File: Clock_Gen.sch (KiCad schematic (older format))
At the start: 0 parts

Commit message: Added clock gen parts
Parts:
- added C?: C_Small, Capacitor_SMD:C_0603_1608Metric_Pad1.08x0.95mm_HandSolder, symbol Device:C_Small
- added C?: C_Polarized_Small, Capacitor_Tantalum_SMD:CP_EIA-1608-10_AVX-L_Pad1.25x1.05mm_HandSolder, symbol Device:C_Polarized_Small
- added C?: C_Small, symbol Device:C_Small
- added C? (x8): 100nF, Capacitor_SMD:C_0201_0603Metric_Pad0.64x0.40mm_HandSolder, symbol Device:C_Small
- added C? (x5): 1uF, Capacitor_SMD:C_0603_1608Metric_Pad1.08x0.95mm_HandSolder, symbol Device:C_Small
- added R?: R_Small_US, Resistor_SMD:R_0603_1608Metric_Pad0.98x0.95mm_HandSolder, symbol Device:R_Small_US
- added U?: Si5344A-D, Package_DFN_QFN:QFN-44-1EP_7x7mm_P0.5mm_EP5.2x5.2mm, symbol Timer_PLL:Si5344A-D
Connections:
- new net: C?.2, U?.19 (OUT0b)
- new net: C?.2, U?.20 (OUT0)
- new net: C?.2, U?.24 (OUT1b)
- new net: C?.2, U?.25 (OUT1)
- new net: C?.2, U?.30 (OUT2b)
- new net: C?.2, U?.31 (OUT2)
- new net: C?.2, U?.35 (OUT3b)
- new net: C?.2, U?.36 (OUT3)
- new net CLK_OUT0_N: C?.1
- new net CLK_OUT0_P: C?.1
- new net CLK_OUT1_N: C?.1
- new net CLK_OUT1_P: C?.1
- new net CLK_OUT2_N: C?.1
- new net CLK_OUT2_P: C?.1
- new net CLK_OUT3_N: C?.1
- new net CLK_OUT3_P: C?.1
- new net GNDD: C?.2, C?.2, C?.2, C?.2, C?.2
- new net VCC1V8: C?.1, C?.1, C?.1, C?.1, C?.1, U?.18 (VDDO0), U?.21 (VDD), U?.23 (VDDO1), U?.26 (VDDS), U?.29 (VDDO2), U?.32 (VDD), U?.34 (VDDO3), U?.39 (VDD), U?.40 (VDD)
- new net VCC3V3: U?.8 (VDDA), U?.9 (VDDA)

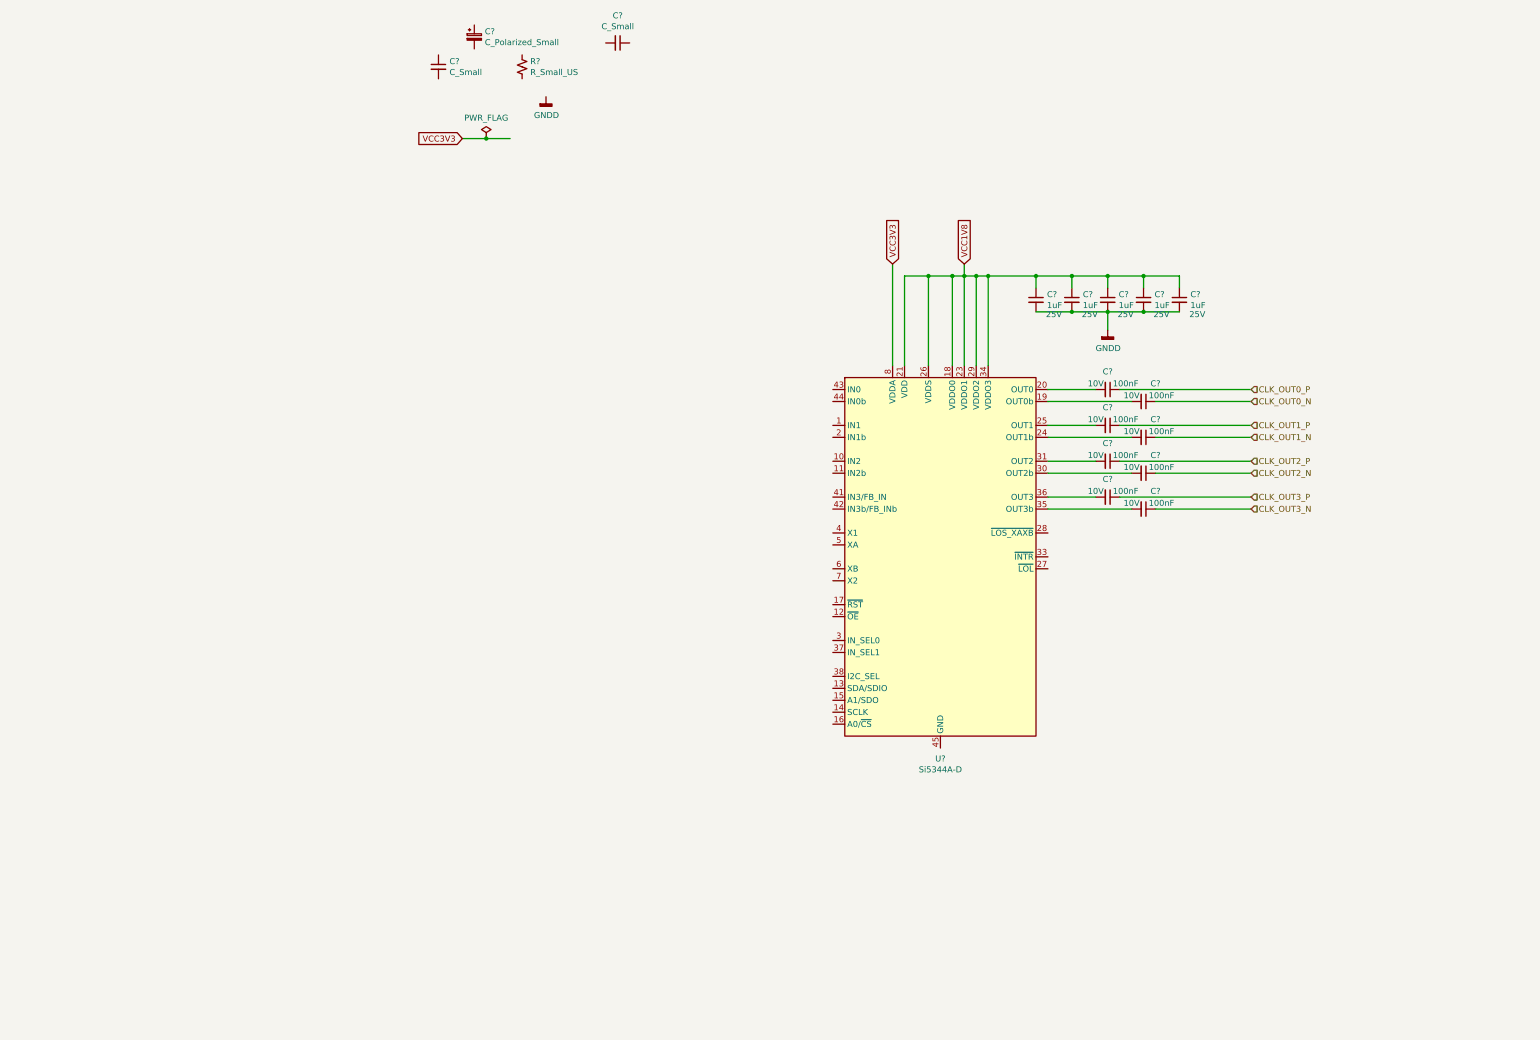
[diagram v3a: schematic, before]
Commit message: Drawn configuration cct of Ethernet PHY Drawn Clock Gen cct
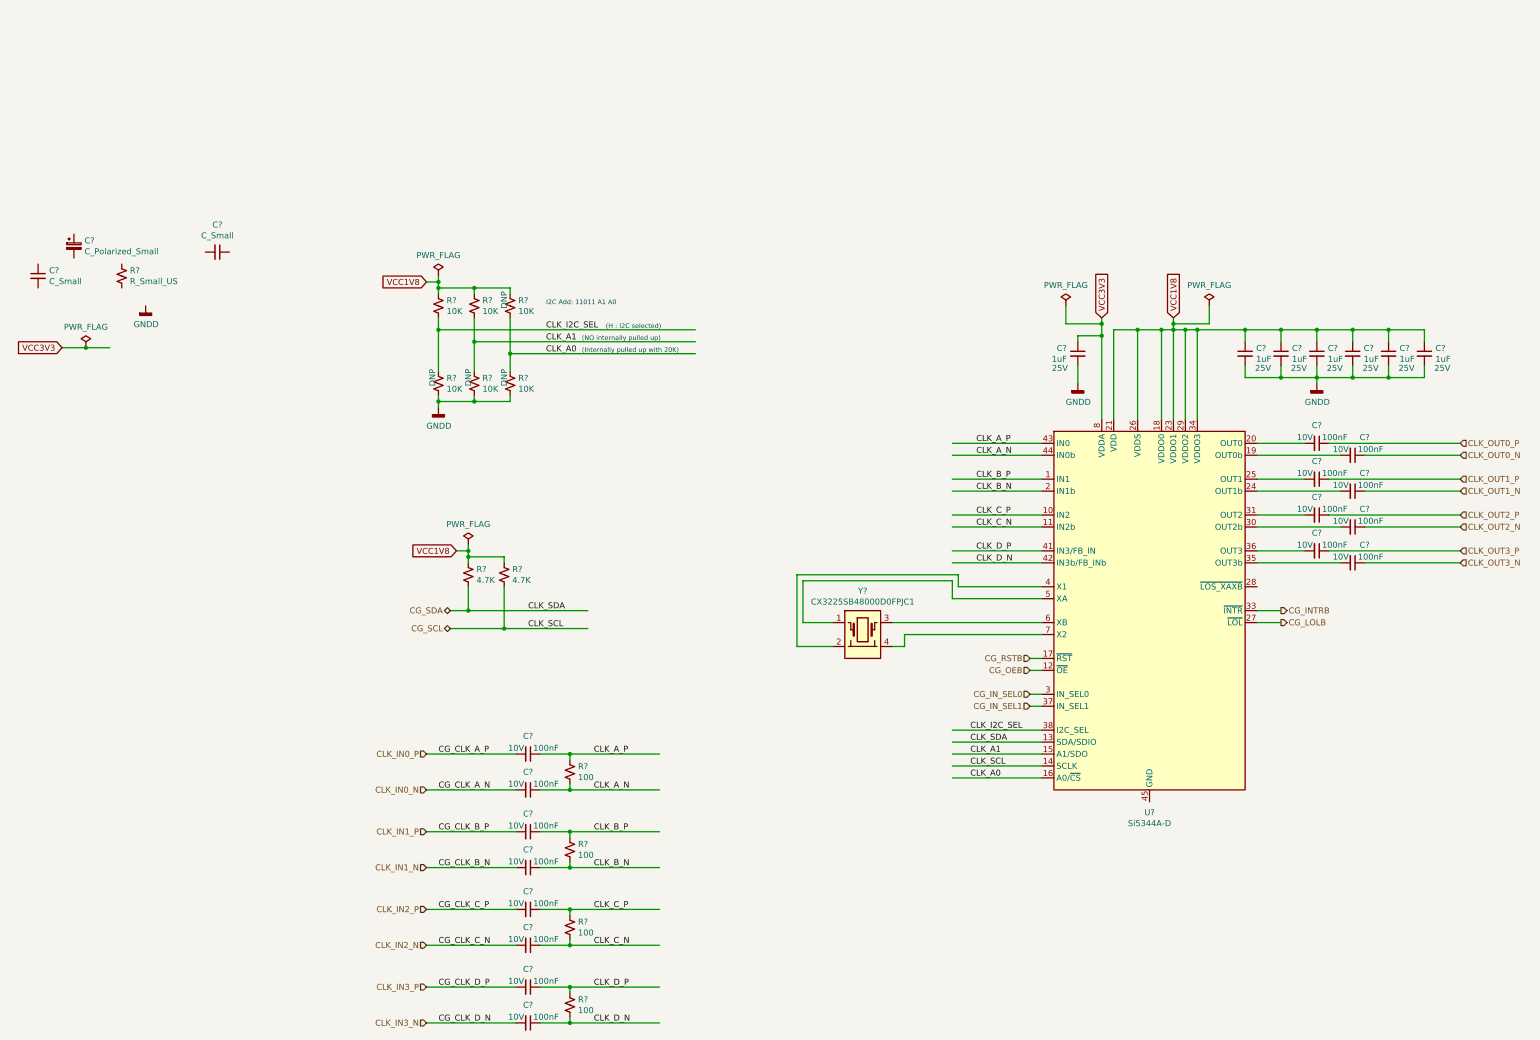
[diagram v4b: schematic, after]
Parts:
- added C? (x8): 100nF, Capacitor_SMD:C_0201_0603Metric_Pad0.64x0.40mm_HandSolder, symbol Device:C_Small
- added C? (x2): 1uF, Capacitor_SMD:C_0603_1608Metric_Pad1.08x0.95mm_HandSolder, symbol Device:C_Small
- added R? (x4): 100, Resistor_SMD:R_0603_1608Metric_Pad0.98x0.95mm_HandSolder, symbol Device:R_Small_US
- added R? (x6): 10K, Resistor_SMD:R_0603_1608Metric_Pad0.98x0.95mm_HandSolder, symbol Device:R_Small_US
- added R? (x2): 4.7K, Resistor_SMD:R_0603_1608Metric_Pad0.98x0.95mm_HandSolder, symbol Device:R_Small_US
- added Y?: CX3225SB48000D0FPJC1, GM_Crystals_Oscilators_n_Resonators:OSCCC320X250X60N, symbol GM_Crystals_Oscilators_n_Resonators:CX3225SB48000D0FPJC1
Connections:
- net labels added: CG_CLK_A_N, CG_CLK_A_P, CG_CLK_B_N, CG_CLK_B_P, CG_CLK_C_N, CG_CLK_C_P, CG_CLK_D_N, CG_CLK_D_P, CG_INTRB, CG_IN_SEL0, CG_IN_SEL1, CG_LOLB, CG_OEB, CG_RSTB, CG_SCL, CG_SDA, CLK_A0, CLK_A1, CLK_A_N, CLK_A_P, CLK_B_N, CLK_B_P, CLK_C_N, CLK_C_P, CLK_D_N, CLK_D_P, CLK_I2C_SEL, CLK_IN0_N, CLK_IN0_P, CLK_IN1_N, CLK_IN1_P, CLK_IN2_N, CLK_IN2_P, CLK_IN3_N, CLK_IN3_P, CLK_SCL, CLK_SDA
- wire segments 46 -> 165
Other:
- note added: "(H : I2C selected)"
- note added: "(Internally pulled up with 20K)"
- note added: "(NO internally pulled up)"
- note added: "I2C Add: 11011 A1 A0"
- moved on the sheet: C?, R?, U?

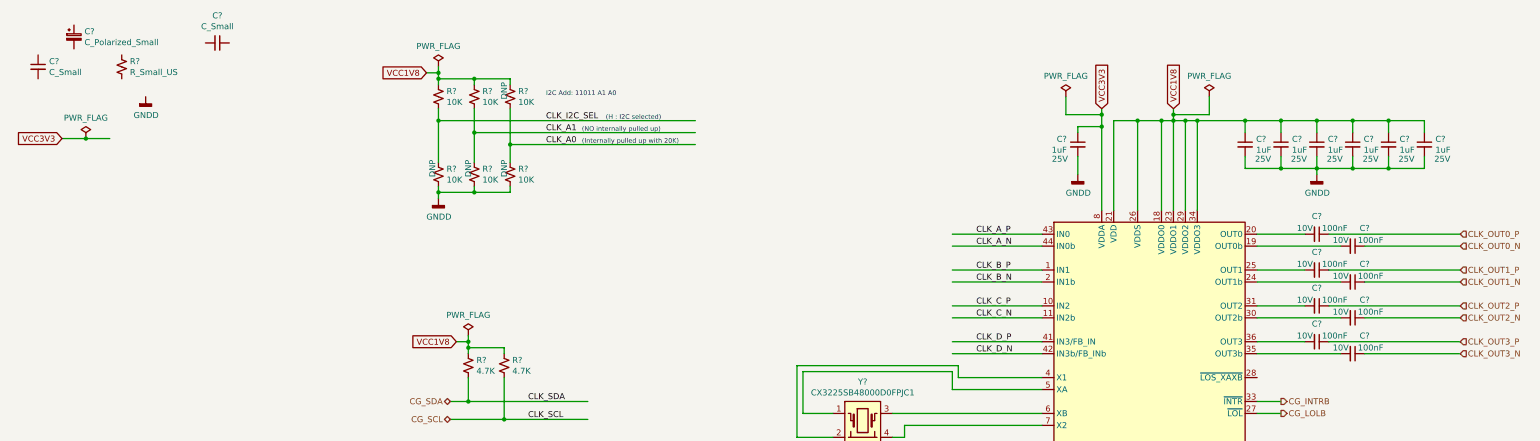
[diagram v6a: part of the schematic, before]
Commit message: Added bus lines -ETH_PHY_CONN -RAM -USB2 Made Output the port direction of clkout of Clock_Gen Placed sheet entris of sheet symbols on top sheet
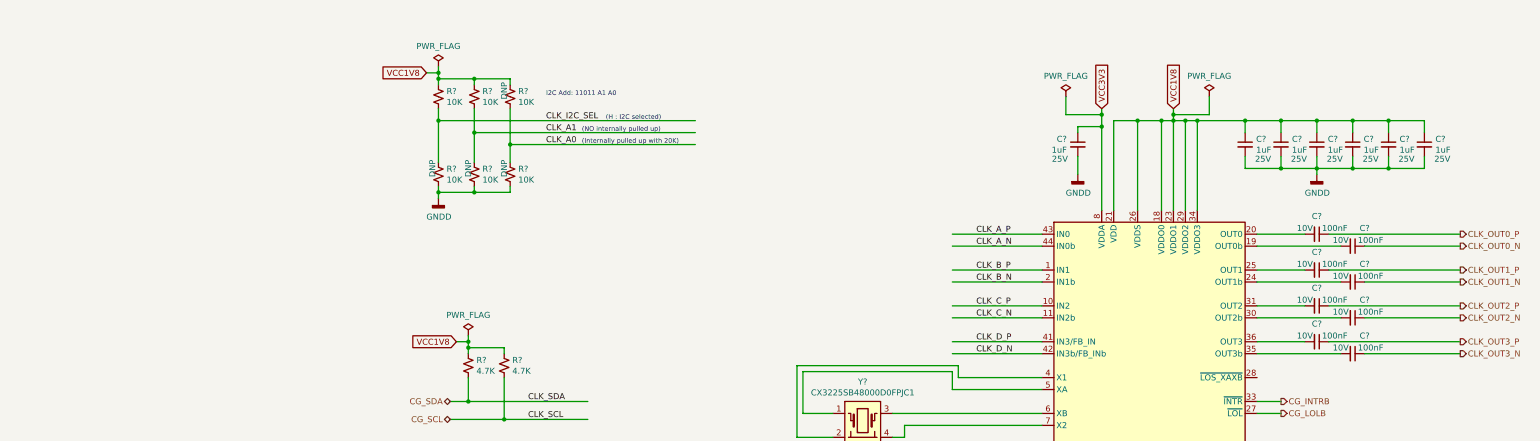
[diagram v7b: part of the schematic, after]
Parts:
- removed C?: C_Small, Capacitor_SMD:C_0603_1608Metric_Pad1.08x0.95mm_HandSolder, symbol Device:C_Small
- removed C?: C_Polarized_Small, Capacitor_Tantalum_SMD:CP_EIA-1608-10_AVX-L_Pad1.25x1.05mm_HandSolder, symbol Device:C_Polarized_Small
- removed C?: C_Small, symbol Device:C_Small
- removed R?: R_Small_US, Resistor_SMD:R_0603_1608Metric_Pad0.98x0.95mm_HandSolder, symbol Device:R_Small_US
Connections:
- wire segments 165 -> 163
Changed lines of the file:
@@
 $Descr A4 11693 8268
 encoding utf-8
-Sheet 5 19
+Sheet 5 20
 Title "CGMPCX1006"
 Date "2021-02-03"
@@
 Comment4 ""
 $EndDescr
-$Comp
-L Device:R_Small_US R?
-U 1 1 6028FC9B
-P -1250 1050
-AR Path="/601E7C5A/6028FC9B" Ref="R?"  Part="1"
-AR Path="/601E7CC8/6028FC9B" Ref="R?"  Part="1"
-AR Path="/601E7C92/6028FC9B" Ref="R?"  Part="1"
-AR Path="/601E7C92/60257FE5/6028FC9B" Ref="R?"  Part="1"
-AR Path="/601E7B38/6028FC9B" Ref="R?"  Part="1"
-F 0 "R?" H -1182 1096 50  0000 L CNN
-F 1 "R_Small_US" H -1182 1005 50  0000 L CNN
-F 2 "Resistor_SMD:R_0603_1608Metric_Pad0.98x0.95mm_HandSolder" H -1250 1050 50  0001 C CNN
-F 3 "~" H -1250 1050 50  0001 C CNN
-	1    -1250 1050
-	1    0    0    -1
-$EndComp
-$Comp
-L Device:C_Small C?
-U 1 1 6028FCA2
-P -1950 1050
-AR Path="/601E7C5A/6028FCA2" Ref="C?"  Part="1"
-AR Path="/601E7CC8/6028FCA2" Ref="C?"  Part="1"
-AR Path="/601E7C92/6028FCA2" Ref="C?"  Part="1"
-AR Path="/601E7C92/60257FE5/6028FCA2" Ref="C?"  Part="1"
-AR Path="/601E7B38/6028FCA2" Ref="C?"  Part="1"
-F 0 "C?" H -1858 1096 50  0000 L CNN
-F 1 "C_Small" H -1858 1005 50  0000 L CNN
-F 2 "Capacitor_SMD:C_0603_1608Metric_Pad1.08x0.95mm_HandSolder" H -1950 1050 50  0001 C CNN
-F 3 "~" H -1950 1050 50  0001 C CNN
-F 4 "" H -1950 1050 50  0000 C CNN "Voltage"
-	1    -1950 1050
-	1    0    0    -1
-$EndComp
-Text GLabel -1750 1650 0    50   Input ~ 0
-VCC3V3
-$Comp
-L power:PWR_FLAG #FLG?
-U 1 1 6028FCA9
-P -1550 1650
-AR Path="/601E7C5A/6028FCA9" Ref="#FLG?"  Part="1"
-AR Path="/601E7CC8/6028FCA9" Ref="#FLG?"  Part="1"
-AR Path="/601E7C92/6028FCA9" Ref="#FLG?"  Part="1"
-AR Path="/601E7C92/60257FE5/6028FCA9" Ref="#FLG?"  Part="1"
-AR Path="/601E7B38/6028FCA9" Ref="#FLG?"  Part="1"
-F 0 "#FLG?" H -1550 1725 50  0001 C CNN
-F 1 "PWR_FLAG" H -1550 1823 50  0000 C CNN
-F 2 "" H -1550 1650 50  0001 C CNN
-F 3 "~" H -1550 1650 50  0001 C CNN
-	1    -1550 1650
-	1    0    0    -1
-$EndComp
-Connection ~ -1550 1650
-Wire Wire Line
-	-1550 1650 -1350 1650
-Wire Wire Line
-	-1750 1650 -1550 1650
-$Comp
-L power:GNDD #PWR?
-U 1 1 6028FCB2
-P -1050 1300
-AR Path="/601DF0A6/6028FCB2" Ref="#PWR?"  Part="1"
-AR Path="/601E7C5A/6028FCB2" Ref="#PWR?"  Part="1"
-AR Path="/601E7CC8/6028FCB2" Ref="#PWR?"  Part="1"
-AR Path="/601E7C92/6028FCB2" Ref="#PWR?"  Part="1"
-AR Path="/601E7C92/60257FE5/6028FCB2" Ref="#PWR?"  Part="1"
-AR Path="/601E7B38/6028FCB2" Ref="#PWR?"  Part="1"
-F 0 "#PWR?" H -1050 1050 50  0001 C CNN
-F 1 "GNDD" H -1046 1145 50  0000 C CNN
-F 2 "" H -1050 1300 50  0001 C CNN
-F 3 "" H -1050 1300 50  0001 C CNN
-	1    -1050 1300
-	1    0    0    -1
-$EndComp
-$Comp
-L Device:C_Polarized_Small C?
-U 1 1 6028FCB9
-P -1650 800
-AR Path="/601E7C92/6028FCB9" Ref="C?"  Part="1"
-AR Path="/601E7C92/60257FE5/6028FCB9" Ref="C?"  Part="1"
-AR Path="/601E7B38/6028FCB9" Ref="C?"  Part="1"
-F 0 "C?" H -1562 846 50  0000 L CNN
-F 1 "C_Polarized_Small" H -1562 755 50  0000 L CNN
-F 2 "Capacitor_Tantalum_SMD:CP_EIA-1608-10_AVX-L_Pad1.25x1.05mm_HandSolder" H -1650 800 50  0001 C CNN
-F 3 "~" H -1650 800 50  0001 C CNN
-F 4 "" H -1650 800 50  0000 C CNN "Voltage"
-	1    -1650 800
-	1    0    0    -1
-$EndComp
-$Comp
-L Device:C_Small C?
-U 1 1 60291703
-P -450 850
-F 0 "C?" V -679 850 50  0000 C CNN
-F 1 "C_Small" V -588 850 50  0000 C CNN
-F 2 "" H -450 850 50  0001 C CNN
-F 3 "~" H -450 850 50  0001 C CNN
-	1    -450 850
-	0    1    1    0
-$EndComp
 $Comp
 L Device:R_Small_US R?
@@
 	1    0    0    -1
 $EndComp
-Text HLabel 9950 2550 2    50   Input ~ 0
+Text HLabel 9950 2550 2    50   Output ~ 0
 CLK_OUT0_N
-Text HLabel 9950 2450 2    50   Input ~ 0
+Text HLabel 9950 2450 2    50   Output ~ 0
 CLK_OUT0_P
-Text HLabel 9950 2850 2    50   Input ~ 0
+Text HLabel 9950 2850 2    50   Output ~ 0
 CLK_OUT1_N
-Text HLabel 9950 2750 2    50   Input ~ 0
+Text HLabel 9950 2750 2    50   Output ~ 0
 CLK_OUT1_P
-Text HLabel 9950 3150 2    50   Input ~ 0
+Text HLabel 9950 3150 2    50   Output ~ 0
 CLK_OUT2_N
-Text HLabel 9950 3050 2    50   Input ~ 0
+Text HLabel 9950 3050 2    50   Output ~ 0
 CLK_OUT2_P
-Text HLabel 9950 3450 2    50   Input ~ 0
+Text HLabel 9950 3450 2    50   Output ~ 0
 CLK_OUT3_N
-Text HLabel 9950 3350 2    50   Input ~ 0
+Text HLabel 9950 3350 2    50   Output ~ 0
 CLK_OUT3_P
 Wire Wire Line
